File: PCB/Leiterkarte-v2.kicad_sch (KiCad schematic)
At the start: 40 parts

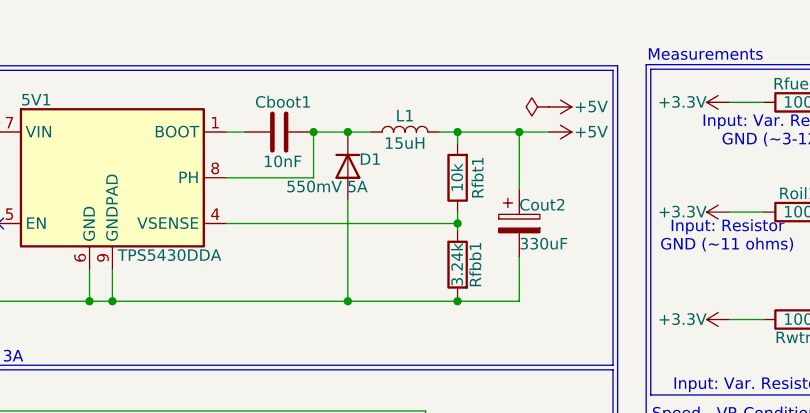
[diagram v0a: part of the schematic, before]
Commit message: Added list of trustworthy manufacturers; Replaced inductor L1
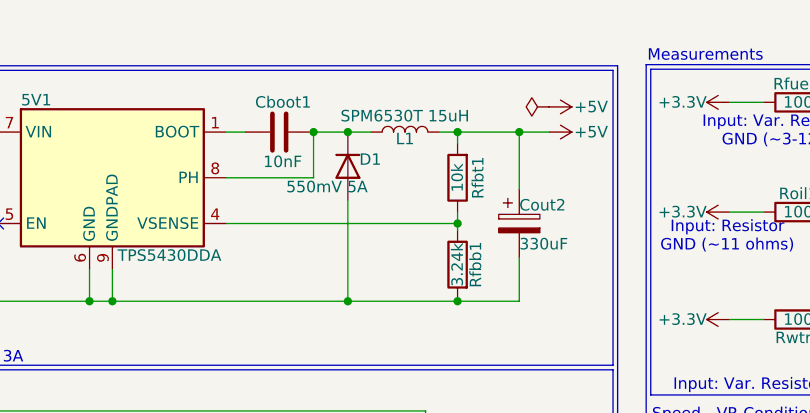
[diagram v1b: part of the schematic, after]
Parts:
- L1: value 15uH -> SPM6530T 15uH; footprint FXL0630-1R5-M:INDM7066X300N -> SPM6530T:IND_SPM6530T-150M-HZ
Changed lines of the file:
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@@
+	)
+	(symbol
+		(lib_id "Device:L")
+		(at 91.694 26.162 90)
+		(unit 1)
+		(exclude_from_sim no)
+		(in_bom yes)
+		(on_board yes)
+		(dnp no)
+		(property "Reference" "L1"
+			(at 91.694 26.924 90)
+			(effects
+				(font
+					(size 1.27 1.27)
+				)
+			)
+		)
+		(property "Value" "SPM6530T 15uH"
+			(at 91.694 24.384 90)
+			(effects
+				(font
+					(size 1.27 1.27)
+				)
+			)
+		)
+		(property "Footprint" "SPM6530T:IND_SPM6530T-150M-HZ"
+			(at 91.694 26.162 0)
+			(effects
+				(font
+					(size 1.27 1.27)
+				)
+				(hide yes)
+			)
+		)
+		(property "Datasheet" "~"
+			(at 91.694 26.162 0)
+			(effects
+				(font
+					(size 1.27 1.27)
+				)
+				(hide yes)
+			)
+		)
+		(property "Description" "Inductor"
+			(at 91.694 26.162 0)
+			(effects
+				(font
+					(size 1.27 1.27)
+				)
+				(hide yes)
+			)
+		)
+		(pin "2"
+		)
+		(pin "1"
+		)
+		(instances
+			(project ""
+				(path "/7159fc5a-6328-470f-acd9-3e0a0aa6e60c"
+					(reference "L1")
+					(unit 1)
+				)
+			)
+		)
 	)
 	(symbol
@@
 					(unit 1)
 				)
-			)
-		)
-	)
-	(symbol
-		(lib_id "Device:L")
-		(at 91.694 26.162 90)
-		(unit 1)
-		(exclude_from_sim no)
-		(in_bom yes)
-		(on_board yes)
-		(dnp no)
-		(property "Reference" "L1"
-			(at 91.694 24.384 90)
-			(effects
-				(font
-					(size 1.27 1.27)
-				)
-			)
-		)
-		(property "Value" "15uH"
-			(at 91.694 27.432 90)
-			(effects
-				(font
-					(size 1.27 1.27)
-				)
-			)
-		)
-		(property "Footprint" "FXL0630-1R5-M:INDM7066X300N"
-			(at 91.694 26.162 0)
-			(effects
-				(font
-					(size 1.27 1.27)
-				)
-				(hide yes)
-			)
-		)
-		(property "Datasheet" "~"
-			(at 91.694 26.162 0)
-			(effects
-				(font
-					(size 1.27 1.27)
-				)
-				(hide yes)
-			)
-		)
-		(property "Description" "Inductor"
-			(at 91.694 26.162 0)
-			(effects
-				(font
-					(size 1.27 1.27)
-				)
-				(hide yes)
-			)
-		)
-		(pin "2"
-		)
-		(pin "1"
-		)
-		(instances
-			(project "Leiterkarte-v2"
-				(path "/7159fc5a-6328-470f-acd9-3e0a0aa6e60c"
-					(reference "L1")
-					(unit 1)
-				)

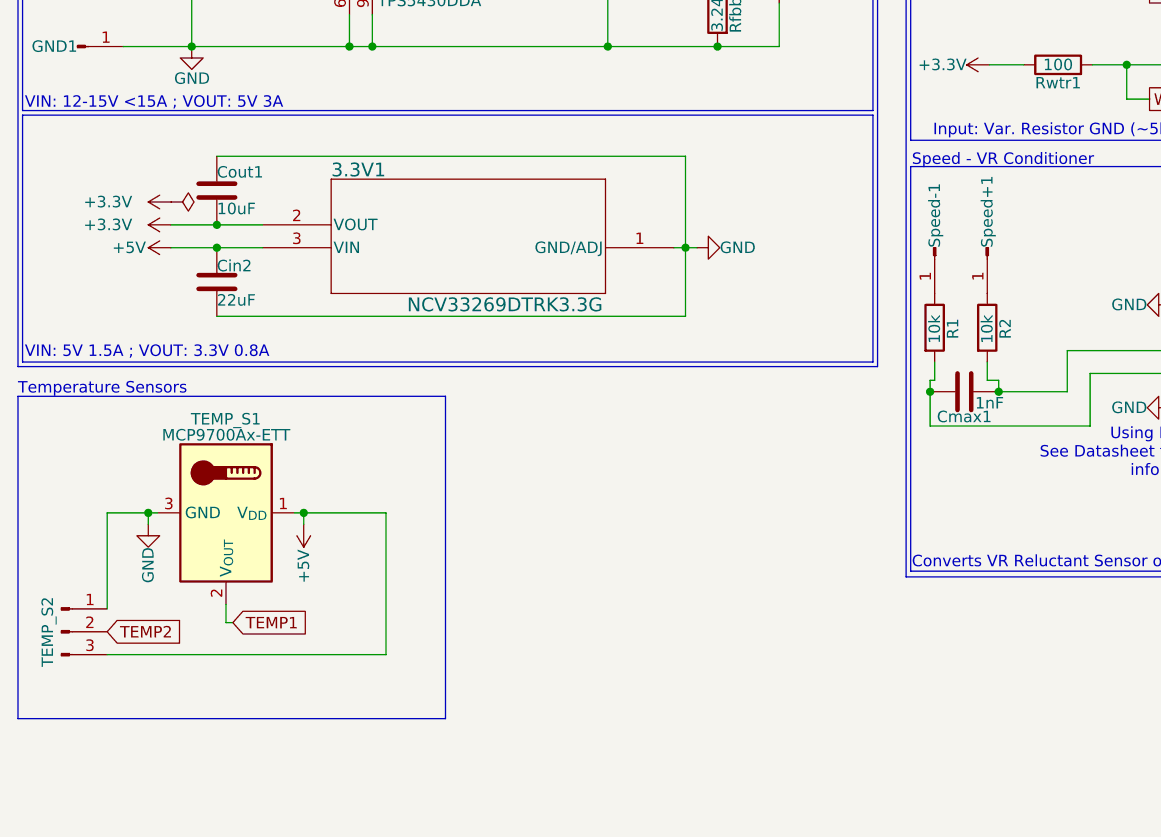
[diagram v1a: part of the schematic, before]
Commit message: Replaced Speed- and Speed+ solder faces with JST SH connector
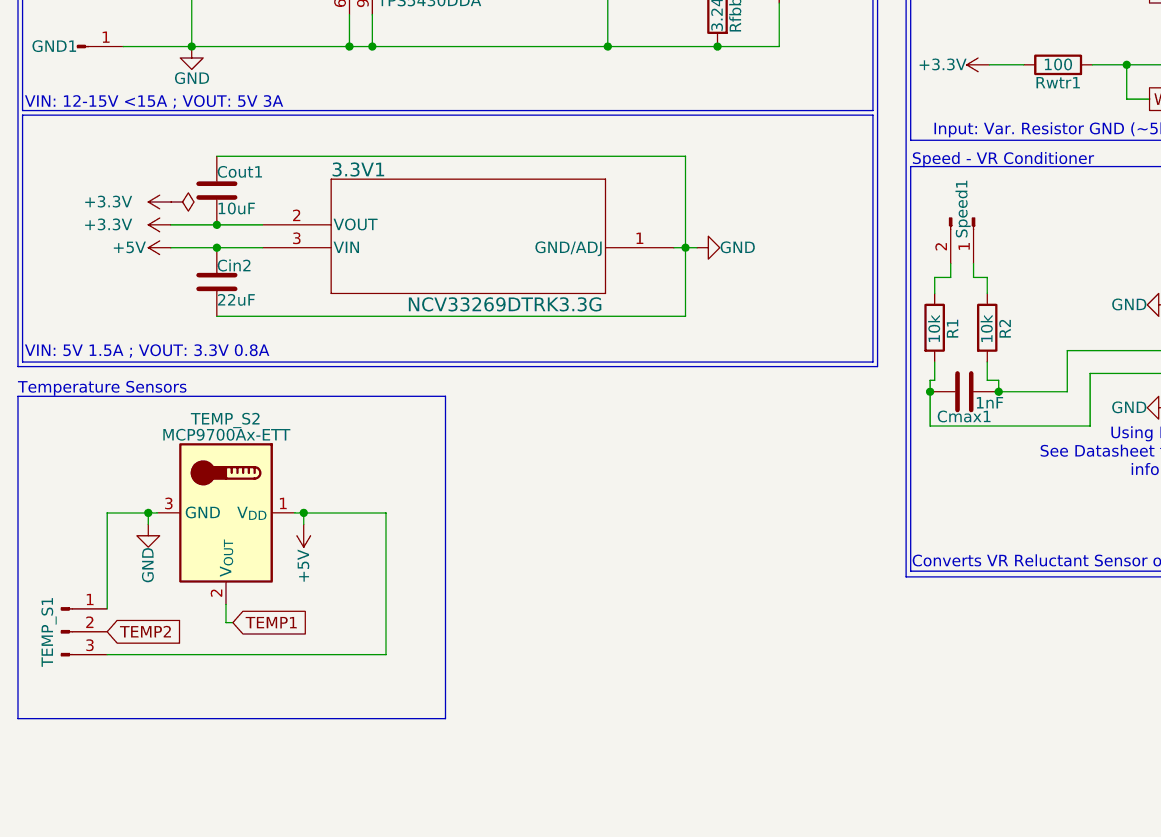
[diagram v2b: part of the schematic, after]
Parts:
- removed Speed+1, Speed-1: Conn_01x01_Pin, Connector_PinHeader_2.54mm:PinHeader_1x01_P2.54mm_Vertical, symbol Connector:Conn_01x01_Pin
- added Speed1: Conn_01x02_Pin, Connector_JST:JST_SH_BM02B-SRSS-TB_1x02-1MP_P1.00mm_Vertical, symbol Connector:Conn_01x02_Pin
- renumbered TEMP_S2 to TEMP_S1, TEMP_S1 to TEMP_S2
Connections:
- net at R2.1: now also Speed1.1 (Pin_1)
- net at R1.1: now also Speed1.2 (Pin_2)
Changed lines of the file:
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@@
 	(wire
 		(pts
+			(xy 125.984 70.612) (xy 125.984 69.088)
+		)
+		(stroke
+			(width 0)
+			(type default)
+		)
+	)
+	(wire
+		(pts
 			(xy 85.344 44.958) (xy 97.536 44.958)
 		)
@@
 	(wire
 		(pts
+			(xy 127.508 72.39) (xy 127.508 70.612)
+		)
+		(stroke
+			(width 0)
+			(type default)
+		)
+	)
+	(wire
+		(pts
 			(xy 39.116 38.354) (xy 39.116 44.958)
 		)
@@
 	(wire
 		(pts
+			(xy 121.666 70.612) (xy 121.666 72.39)
+		)
+		(stroke
+			(width 0)
+			(type default)
+		)
+	)
+	(wire
+		(pts
 			(xy 41.91 74.93) (xy 93.98 74.93)
 		)
@@
 	(wire
 		(pts
+			(xy 123.444 69.088) (xy 123.444 70.612)
+		)
+		(stroke
+			(width 0)
+			(type default)
+		)
+	)
+	(wire
+		(pts
 			(xy 139.192 46.99) (xy 143.002 46.99)
 		)
@@
 	(wire
 		(pts
+			(xy 123.444 70.612) (xy 121.666 70.612)
+		)
+		(stroke
+			(width 0)
+			(type default)
+		)
+	)
+	(wire
+		(pts
 			(xy 36.83 67.31) (xy 41.91 67.31)
 		)
@@
 	(wire
 		(pts
+			(xy 127.508 70.612) (xy 125.984 70.612)
+		)
+		(stroke
+			(width 0)
+			(type default)
+		)
+	)
+	(wire
+		(pts
 			(xy 211.328 73.66) (xy 211.328 93.98)
 		)
@@
 		(on_board yes)
 		(dnp no)
-		(property "Reference" "TEMP_S2"
+		(property "Reference" "TEMP_S1"
 			(at 23.114 109.982 90)
 			(effects
@@
 			(project ""
 				(path "/7159fc5a-6328-470f-acd9-3e0a0aa6e60c"
-					(reference "TEMP_S2")
+					(reference "TEMP_S1")
 					(unit 1)
 				)
@@
 		(on_board yes)
 		(dnp no)
-		(property "Reference" "TEMP_S1"
+		(property "Reference" "TEMP_S2"
 			(at 42.926 86.36 90)
 			(effects
@@
 			(project "Leiterkarte-v2"
 				(path "/7159fc5a-6328-470f-acd9-3e0a0aa6e60c"
-					(reference "TEMP_S1")
+					(reference "TEMP_S2")
 					(unit 1)
 				)
@@
 	)
 	(symbol
-		(lib_id "Connector:Conn_01x01_Pin")
-		(at 127.508 67.31 270)
-		(unit 1)
-		(exclude_from_sim no)
-		(in_bom yes)
-		(on_board yes)
-		(dnp no)
-		(fields_autoplaced yes)
-		(property "Reference" "Speed+1"
-			(at 127.508 67.31 0)
-			(effects
-				(font
-					(size 1.27 1.27)
-				)
-				(justify right)
-			)
-		)
-		(property "Value" "Conn_01x01_Pin"
-			(at 130.048 67.945 0)
-			(effects
-				(font
-					(size 1.27 1.27)
-				)
-				(hide yes)
-			)
-		)
-		(property "Footprint" "Connector_PinHeader_2.54mm:PinHeader_1x01_P2.54mm_Vertical"
-			(at 127.508 67.31 0)
-			(effects
-				(font
-					(size 1.27 1.27)
-				)
-				(hide yes)
-			)
-		)
-		(property "Datasheet" "~"
-			(at 127.508 67.31 0)
-			(effects
-				(font
-					(size 1.27 1.27)
-				)
-				(hide yes)
-			)
-		)
-		(property "Description" "Generic connector, single row, 01x01, script generated"
-			(at 127.508 67.31 0)
-			(effects
-				(font
-					(size 1.27 1.27)
-				)
-				(hide yes)
-			)
-		)
-		(pin "1"
-		)
-		(instances
-			(project "Leiterkarte-v2"
-				(path "/7159fc5a-6328-470f-acd9-3e0a0aa6e60c"
-					(reference "Speed+1")
-					(unit 1)
-				)
-			)
-		)
-	)
-	(symbol
 		(lib_id "power:PWR_FLAG")
 		(at 31.496 35.814 270)
@@
 	)
 	(symbol
+		(lib_id "Connector:Conn_01x02_Pin")
+		(at 125.984 64.008 270)
+		(unit 1)
+		(exclude_from_sim no)
+		(in_bom yes)
+		(on_board yes)
+		(dnp no)
+		(property "Reference" "Speed1"
+			(at 124.714 62.992 0)
+			(effects
+				(font
+					(size 1.27 1.27)
+				)
+			)
+		)
+		(property "Value" "Conn_01x02_Pin"
+			(at 129.032 64.643 0)
+			(effects
+				(font
+					(size 1.27 1.27)
+				)
+				(hide yes)
+			)
+		)
+		(property "Footprint" "Connector_JST:JST_SH_BM02B-SRSS-TB_1x02-1MP_P1.00mm_Vertical"
+			(at 125.984 64.008 0)
+			(effects
+				(font
+					(size 1.27 1.27)
+				)
+				(hide yes)
+			)
+		)
+		(property "Datasheet" "~"
+			(at 125.984 64.008 0)
+			(effects
+				(font
+					(size 1.27 1.27)
+				)
+				(hide yes)
+			)
+		)
+		(property "Description" "Generic connector, single row, 01x02, script generated"
+			(at 125.984 64.008 0)
+			(effects
+				(font
+					(size 1.27 1.27)
+				)
+				(hide yes)
+			)
+		)
+		(pin "2"
+		)
+		(pin "1"
+		)
+		(instances
+			(project "Leiterkarte-v2"
+				(path "/7159fc5a-6328-470f-acd9-3e0a0aa6e60c"
+					(reference "Speed1")
+					(unit 1)
+				)
+			)
+		)
+	)
+	(symbol
 		(lib_id "Device:R")
 		(at 185.928 22.86 90)
@@
 					(unit 1)
 				)
-			)
-		)
-	)
-	(symbol
-		(lib_id "Connector:Conn_01x01_Pin")
-		(at 121.666 67.31 270)
-		(unit 1)
-		(exclude_from_sim no)
-		(in_bom yes)
-		(on_board yes)
-		(dnp no)
-		(fields_autoplaced yes)
-		(property "Reference" "Speed-1"
-			(at 121.666 67.31 0)
-			(effects
-				(font
-					(size 1.27 1.27)
-				)
-				(justify right)
-			)
-		)
-		(property "Value" "Conn_01x01_Pin"
-			(at 124.206 67.945 0)
-			(effects
-				(font
-					(size 1.27 1.27)
-				)
-				(hide yes)
-			)
-		)
-		(property "Footprint" "Connector_PinHeader_2.54mm:PinHeader_1x01_P2.54mm_Vertical"
-			(at 121.666 67.31 0)
-			(effects
-				(font
-					(size 1.27 1.27)
-				)
-				(hide yes)
-			)
-		)
-		(property "Datasheet" "~"
-			(at 121.666 67.31 0)
-			(effects
-				(font
-					(size 1.27 1.27)
-				)
-				(hide yes)
-			)
-		)
-		(property "Description" "Generic connector, single row, 01x01, script generated"
-			(at 121.666 67.31 0)
-			(effects
-				(font
-					(size 1.27 1.27)
-				)
-				(hide yes)
-			)
-		)
-		(pin "1"
-		)
-		(instances
-			(project "Leiterkarte-v2"
-				(path "/7159fc5a-6328-470f-acd9-3e0a0aa6e60c"
-					(reference "Speed-1")
-					(unit 1)
-				)

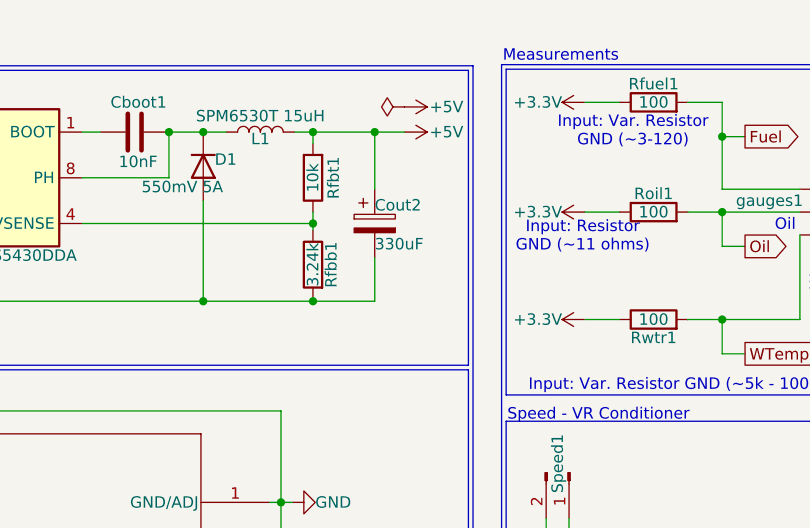
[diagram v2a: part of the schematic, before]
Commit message: Replaced capacitor Cout2 and moved it to other side of the PCB;Updated some resistor footprints (to 0805);Some other stuff I forgot but similar :)
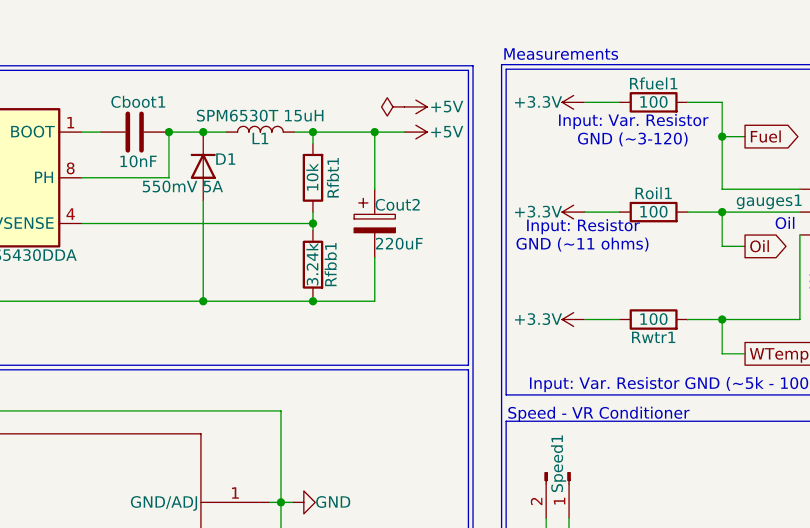
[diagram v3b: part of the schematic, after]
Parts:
- Cout2: value 330uF -> 220uF; footprint Capacitor_SMD:C_0805_2012Metric -> Capacitor_SMD:CP_Elec_6.3x5.9
- D1: footprint Diode_SMD:D_0805_2012Metric -> Diode_SMD:D_SMA
- R1, R2: footprint Resistor_SMD:R_0603_1608Metric -> Resistor_SMD:R_0805_2012Metric
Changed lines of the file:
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@@
 			)
 		)
-		(property "Value" "330uF"
+		(property "Value" "220uF"
 			(at 104.394 38.608 0)
 			(effects
@@
 			)
 		)
-		(property "Footprint" "Capacitor_SMD:C_0805_2012Metric"
+		(property "Footprint" "Capacitor_SMD:CP_Elec_6.3x5.9"
 			(at 105.3592 40.132 0)
 			(effects
@@
 			)
 		)
-		(property "Footprint" "Diode_SMD:D_0805_2012Metric"
+		(property "Footprint" "Diode_SMD:D_SMA"
 			(at 85.344 29.972 0)
 			(effects
@@
 			)
 		)
-		(property "Footprint" "Resistor_SMD:R_0603_1608Metric"
+		(property "Footprint" "Resistor_SMD:R_0805_2012Metric"
 			(at 119.888 76.2 90)
 			(effects
@@
 			)
 		)
-		(property "Footprint" "Resistor_SMD:R_0603_1608Metric"
+		(property "Footprint" "Resistor_SMD:R_0805_2012Metric"
 			(at 125.73 76.2 90)
 			(effects

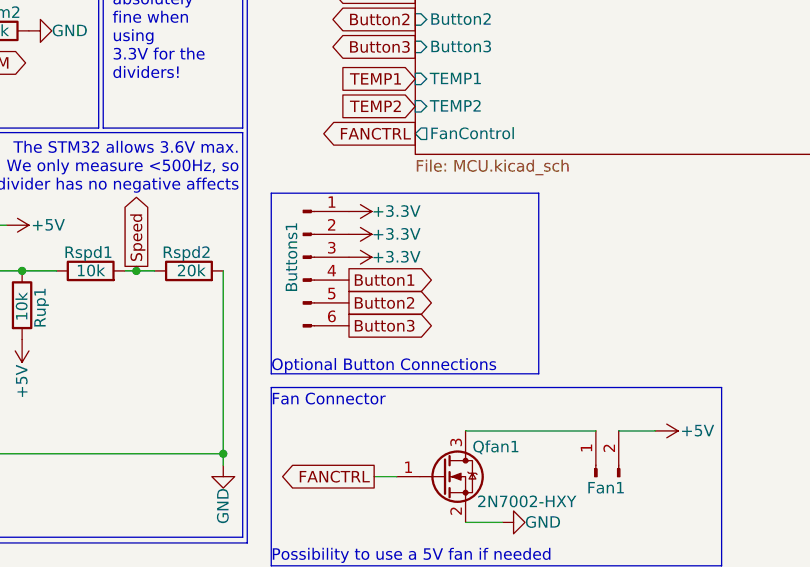
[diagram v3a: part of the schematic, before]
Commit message: Replaced STM32 with ESP32; Addec circuitry for ESP32; Removed LEDs; Added USB-C for flashing
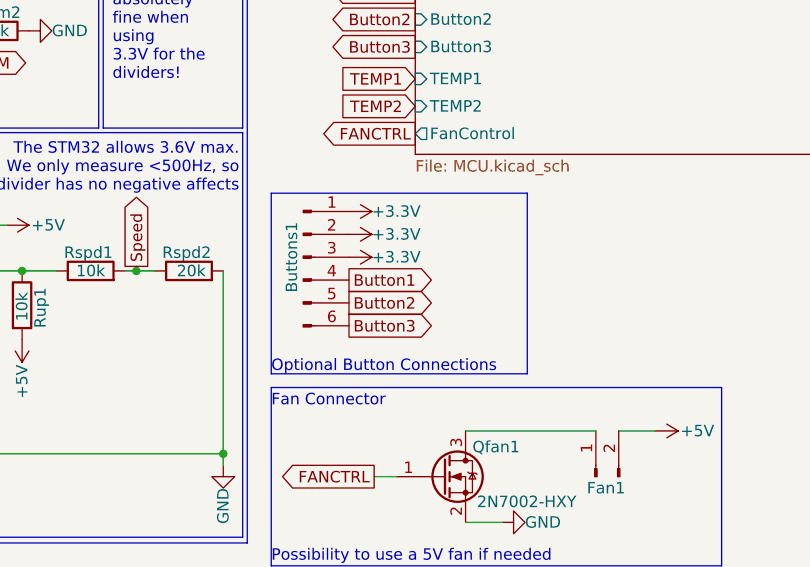
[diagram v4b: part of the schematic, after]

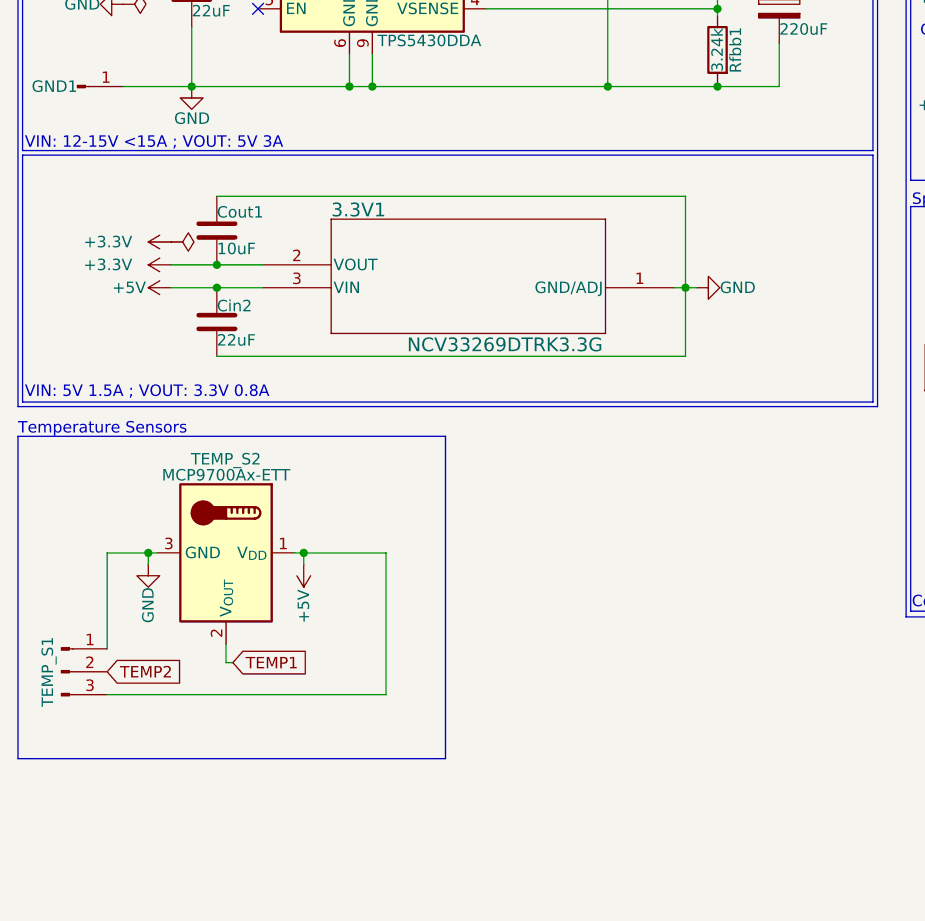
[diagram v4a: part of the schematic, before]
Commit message: Changed PCB design completely; Upgraded 3.3V regulator to 1.5A version; Removed no more needed libaries
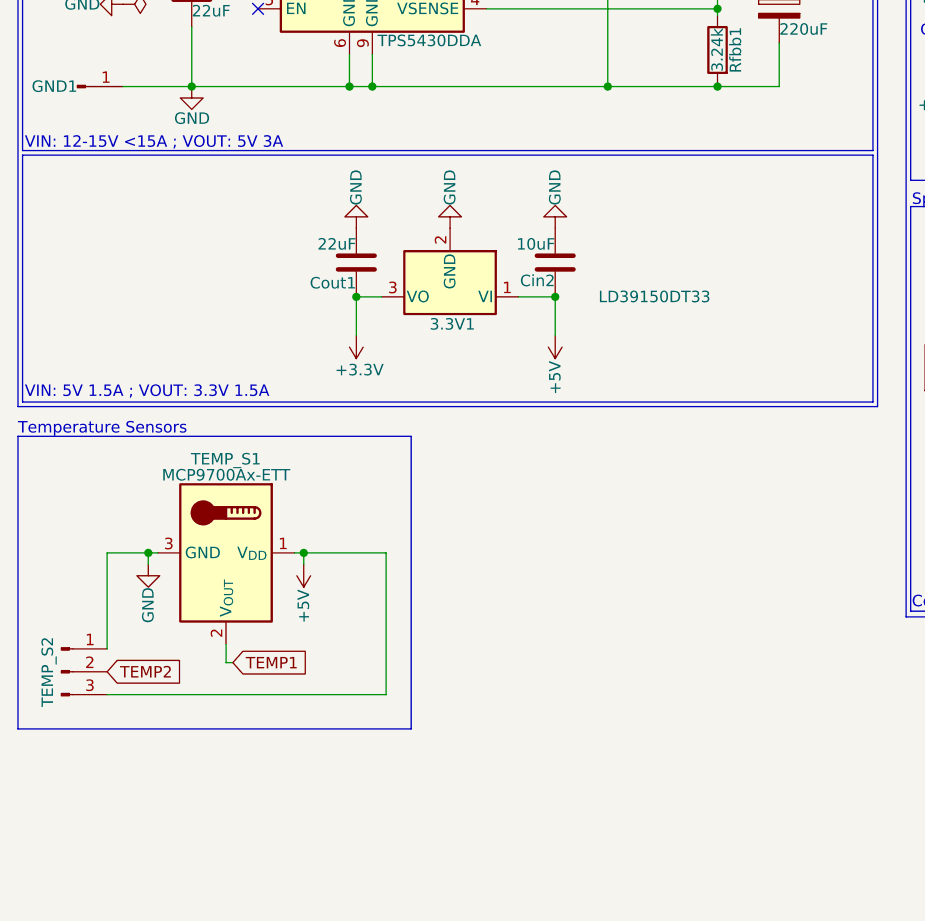
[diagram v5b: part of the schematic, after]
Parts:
- removed 3.3V1: NCV33269DTRK3.3G, NCV33269DTRK3.3G:DPAK-3_ONS-M, symbol NCV33269DTRK3.3G:NCV33269DTRK3.3G
- added 3.3V1: LD39150DT33, Package_TO_SOT_SMD:TO-252-3_TabPin2, symbol Regulator_Linear:LD39150DT33
- Cin2: value 22uF -> 10uF
- Cout1: value 10uF -> 22uF
- F1: footprint Fuse:Fuse_0603_1608Metric -> Fuse:0458Series_LTF-M
- GND1, Vcc1: footprint Connector_PinHeader_2.54mm:PinHeader_1x01_P2.54mm_Vertical -> MountingHole:MountingHole_3.2mm_M3_Pad
- renumbered TEMP_S2 to TEMP_S1, TEMP_S1 to TEMP_S2
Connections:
- net +3.3V: now also Cout1.1, 3.3V1.3 (VO); no longer Cout1.2
- net +5V: now also 3.3V1.1 (VI)
- net GND: now also Cout1.2, 3.3V1.2 (GND); no longer Cout1.1
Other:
- note added: "VIN: 5V 1.5A ; VOUT: 3.3V 1.5A"
- note removed: "VIN: 5V 1.5A ; VOUT: 3.3V 0.8A"
